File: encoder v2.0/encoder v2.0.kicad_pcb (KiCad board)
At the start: 2 copper layers, 40 x 40 mm, 15 parts, among them J1 Conn_01x02, J2 Conn_01x03, J3 Conn_01x05, J4 Conn_01x01, J5 Conn_01x05, U1 74LS14

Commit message: finalizando el ruteo
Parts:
- H1, H2, H3, H4: footprint MountingHole:MountingHole_4mm_Pad_Via -> MountingHole:MountingHole_3mm_Pad
- moved J5 121.0 mm to (111.8, 113.0), turned to 90 degrees
- moved J3 110.6 mm to (132.2, 105.0), turned to 180 degrees
- moved U1 99.3 mm to (119.0, 93.5)
- moved J1 98.8 mm to (101.5, 88.5), turned to 270 degrees
- moved D1 89.3 mm to (101.0, 106.8), turned to 90 degrees
- moved R1 87.8 mm to (98.2, 99.0)
- moved J4 84.3 mm to (112.5, 101.0)
- moved C2 83.4 mm to (122.2, 82.5)
- moved R2 79.5 mm to (112.2, 86.2), turned to 270 degrees
- moved C1 76.1 mm to (126.8, 89.0)
- moved J2 72.2 mm to (112.5, 82.5), turned to 90 degrees
- moved H3 0.90 mm to (131.8, 113.8)
- moved H1 0.71 mm to (99.8, 81.8)
- moved H2 0.71 mm to (131.8, 81.8)
- moved H4 0.71 mm to (99.8, 113.8)
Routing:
- net Net-(J3-Pad1): track 0.00 -> 49.5 mm
- net VCC: track 0.00 -> 49.4 mm, vias 0 -> 2
- net Net-(J3-Pad2): track 0.00 -> 42.8 mm, vias 0 -> 2
- net Net-(C2-Pad1): track 0.00 -> 24.2 mm
- net Net-(J5-Pad5): track 0.00 -> 17.1 mm
- net Net-(J5-Pad4): track 0.00 -> 16.5 mm
- net Net-(J5-Pad3): track 0.00 -> 15.7 mm
- net Net-(J5-Pad1): track 0.00 -> 14.9 mm
- net Net-(D1-Pad1): track 0.00 -> 10.5 mm
- net Net-(J4-Pad1): track 0.00 -> 9.21 mm
- net Net-(J5-Pad2): track 0.00 -> 8.75 mm
- net Net-(J3-Pad3): track 0.00 -> 8.61 mm
- net Net-(J3-Pad4): track 0.00 -> 7.18 mm
- net Net-(J3-Pad5): track 0.00 -> 6.13 mm
- added copper zone on B.Cu, net GND
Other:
- net class Default: clearance 0.2 -> 0.5; trace_width 0.25 -> 0.5; via_dia 0.8 -> 1.6; via_drill 0.4 -> 0.8
- rule trace_clearance: 0.2 -> 0.5

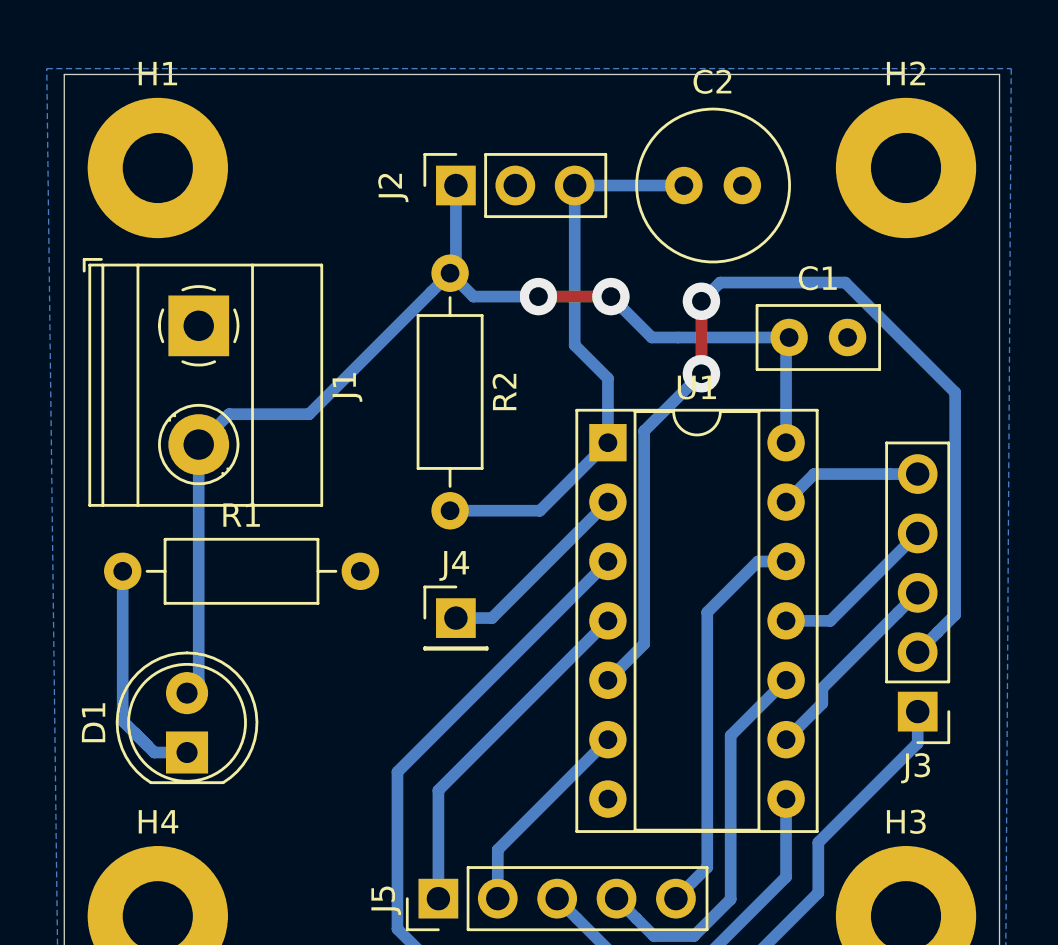
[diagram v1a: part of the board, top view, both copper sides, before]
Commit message: Ruteo finalizado - realizar última verificación
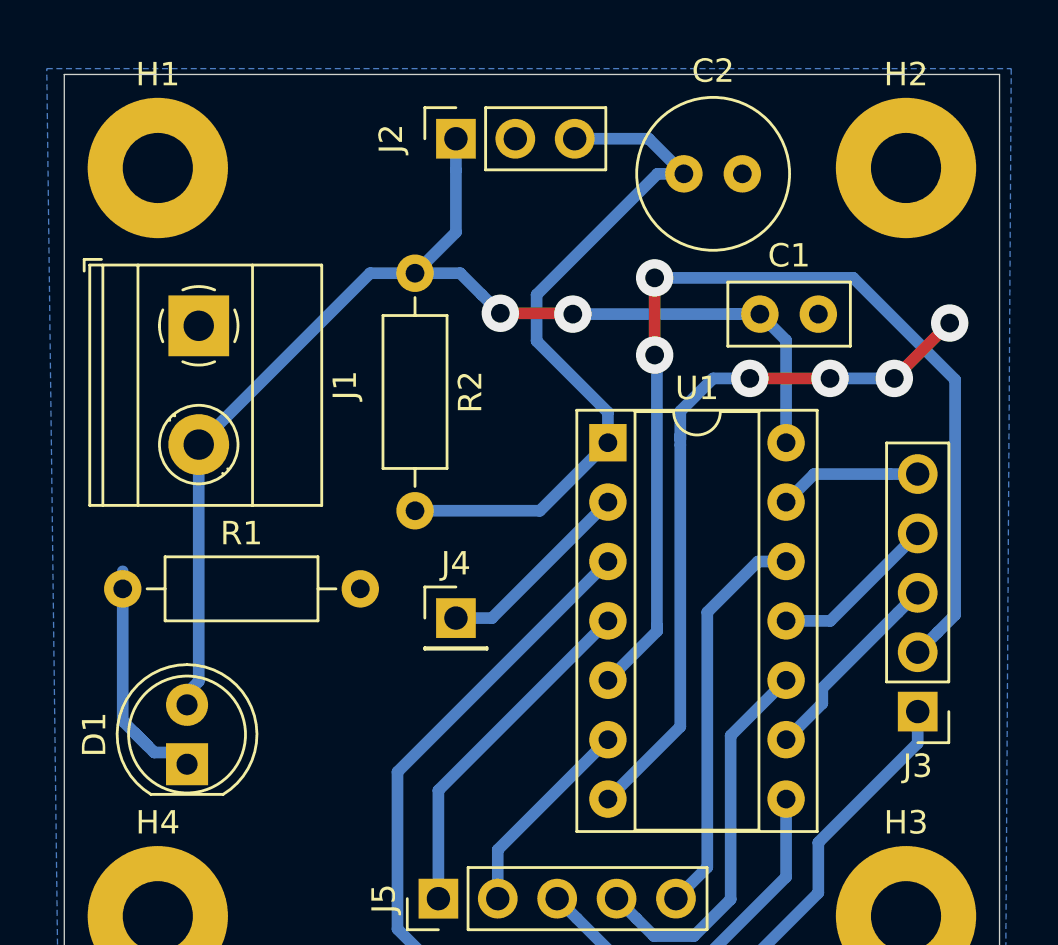
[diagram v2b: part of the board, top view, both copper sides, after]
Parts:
- moved J2 2.00 mm to (112.5, 80.5)
- moved C1 1.60 mm to (125.5, 88.0)
- moved R2 1.50 mm to (110.8, 86.2)
- moved R1 0.75 mm to (98.2, 99.8)
- moved C2 0.50 mm to (122.2, 82.0)
- moved D1 0.50 mm to (101.0, 107.2)
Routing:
- net GND: track 0.00 -> 31.7 mm, vias 0 -> 4
- net Net-(C2-Pad1): track 24.2 -> 30.8 mm
- net VCC: track 49.4 -> 52.6 mm
- net Net-(J3-Pad2): track 42.8 -> 45.3 mm

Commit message: Ruteo finalizado y realizar una verificación
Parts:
- added J6: Conn_01x01, Connector_PinHeader_2.54mm:PinHeader_1x01_P2.54mm_Vertical, F.Cu at (108.8, 88.0)
- added JP1: Jumper_3_Open, Connector_PinHeader_2.54mm:PinHeader_1x03_P2.54mm_Vertical, F.Cu at (117.2, 84.0)
- J1: footprint TerminalBlock_Phoenix:TerminalBlock_Phoenix_MKDS-1,5-2-5.08_1x02_P5.08mm_Horizontal -> Terminal Degson:dg126
- moved J4 9.10 mm to (107.0, 108.2)
- moved J2 5.25 mm to (112.5, 75.2)
- moved H1 5.00 mm to (99.8, 76.8)
- moved H2 5.00 mm to (131.8, 76.8)
- moved C2 4.81 mm to (127.0, 82.8)
- moved R2 4.60 mm to (112.5, 90.5)
- moved J1 1.25 mm to (100.8, 87.5)
- moved D1 1.12 mm to (100.5, 108.2)
- moved J5 0.50 mm to (111.8, 112.5)
- moved R1 0.50 mm to (98.8, 99.8)
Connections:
- J2 pad 3: Net-(C2-Pad1) -> Net-(J2-Pad3)
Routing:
- net GND: track 31.7 -> 10.0 mm
- net VCC: track 52.6 -> 74.0 mm
- net Net-(J2-Pad3): track 0.00 -> 9.94 mm
- net Net-(J4-Pad1): track 9.21 -> 17.3 mm
- net Net-(J6-Pad1): track 0.00 -> 5.87 mm
- net Net-(D1-Pad1): track 10.5 -> 9.47 mm
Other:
- board size 40 x 40 mm -> 40 x 45 mm
